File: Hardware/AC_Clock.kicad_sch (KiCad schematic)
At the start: 49 parts, among them J1 L, J2 N, J5 Conn_01x10, J6 Conn_01x10, SW1 Min_PB, SW2 Hr_PB, T1 10:1, U1 AZ1117-5.0, U2 LTV-817S, U3 4040, U4 74LS393, U5 74LS393

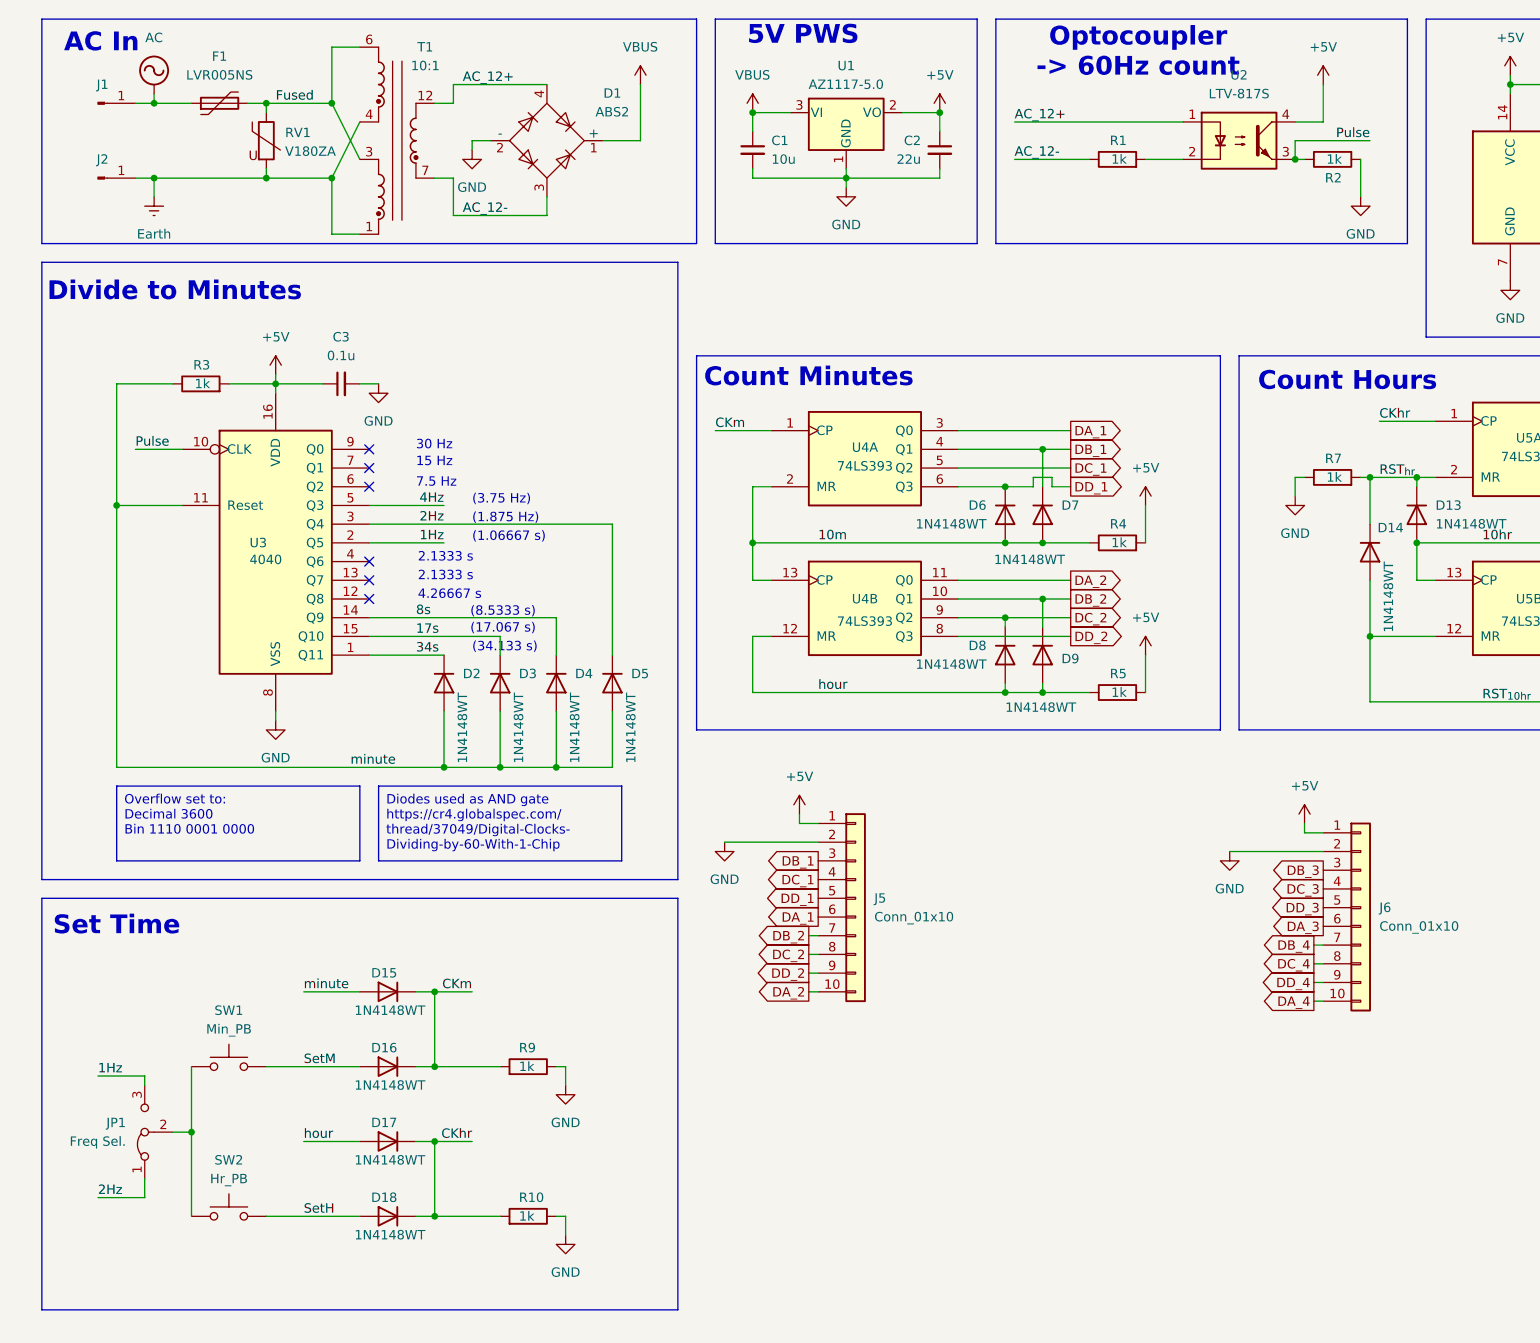
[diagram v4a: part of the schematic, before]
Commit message: Add Class Y Safety capacitor
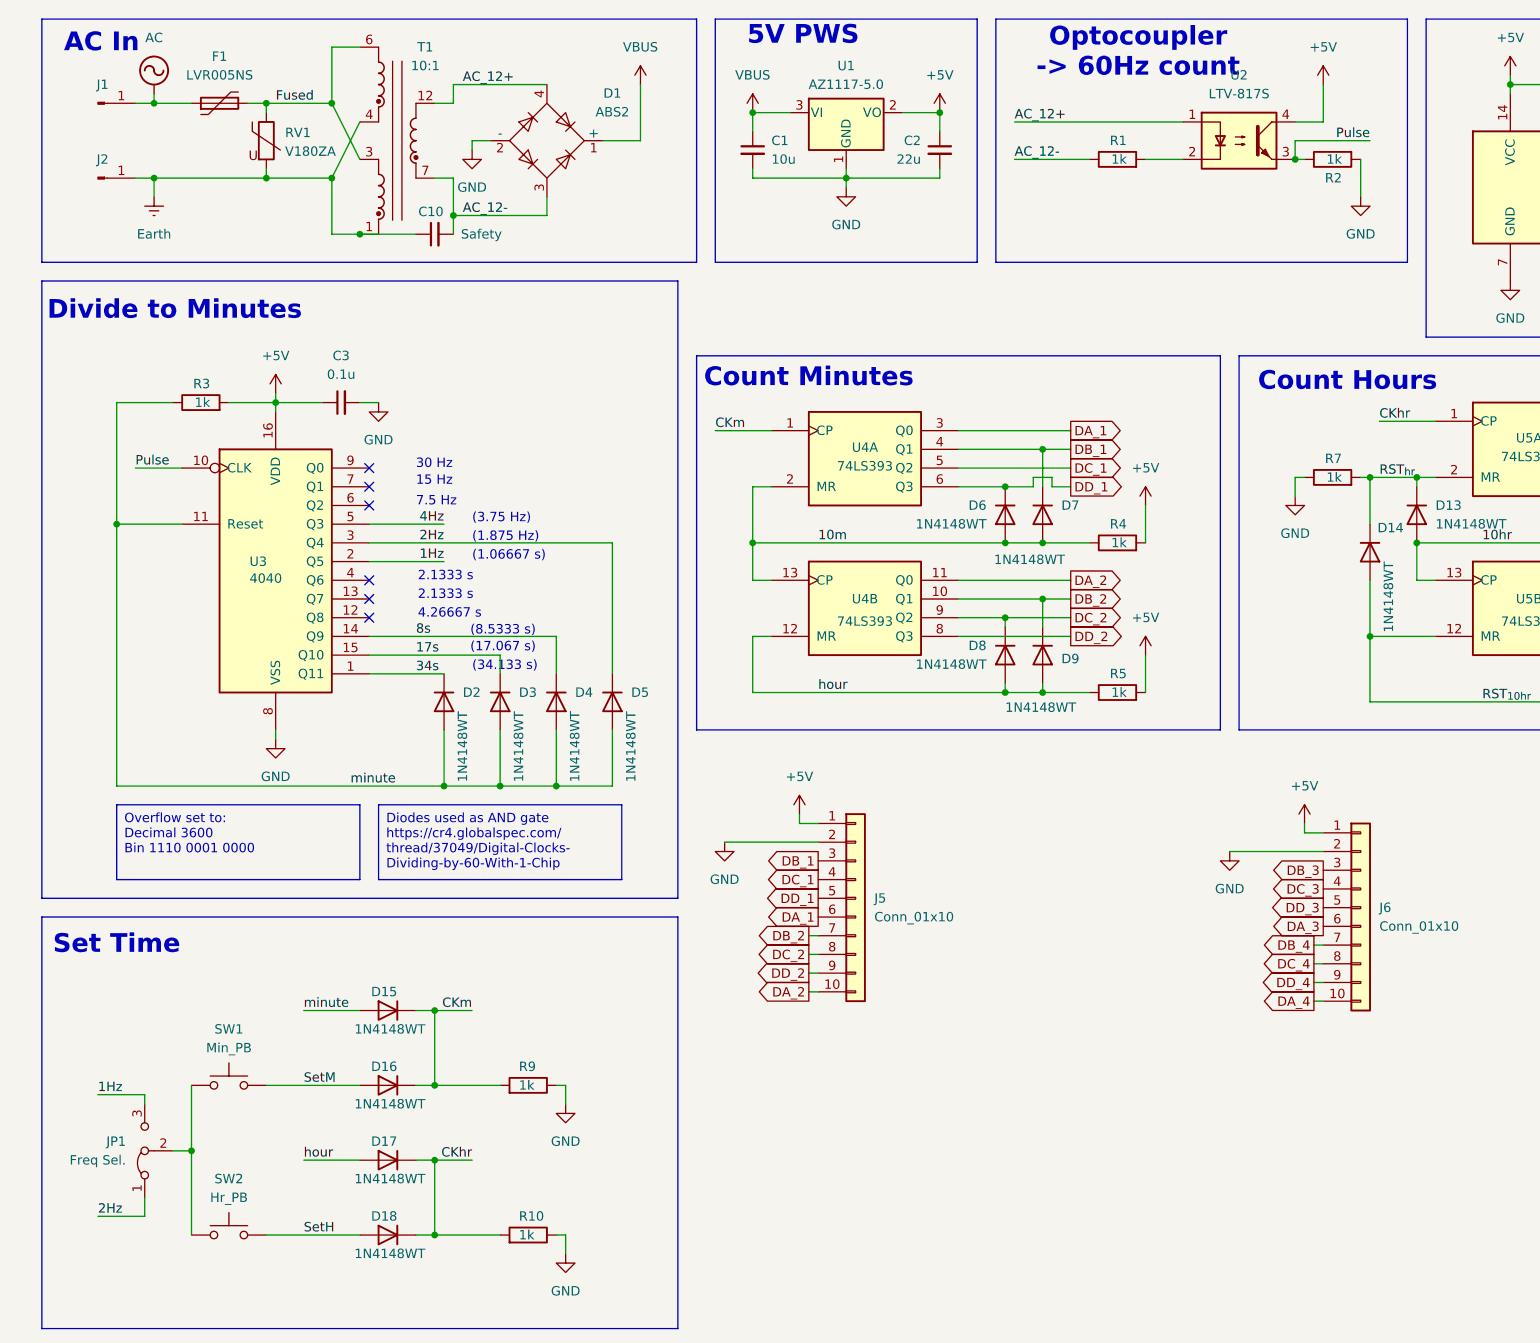
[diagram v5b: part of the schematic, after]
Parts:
- added C10: Safety, Capacitor_THT:C_Disc_D7.5mm_W5.0mm_P7.50mm, symbol Device:C_Small
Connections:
- net AC_12-: now also C10.2
- net Earth: now also C10.1
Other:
- moved on the sheet: C3, D15, D16, D17, D18, D2, D3, D4, D5, JP1, R10, R3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

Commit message: Fix U2 footprint; change to DIP-4
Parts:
- U2: footprint Package_DIP:SMDIP-6_W9.53mm_Clearance8mm -> Package_DIP:SMDIP-4_W9.53mm
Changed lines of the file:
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@@
 			)
 		)
-		(property "Footprint" "Package_DIP:SMDIP-6_W9.53mm_Clearance8mm"
+		(property "Footprint" "Package_DIP:SMDIP-4_W9.53mm"
 			(at 177.8 39.37 0)
 			(effects

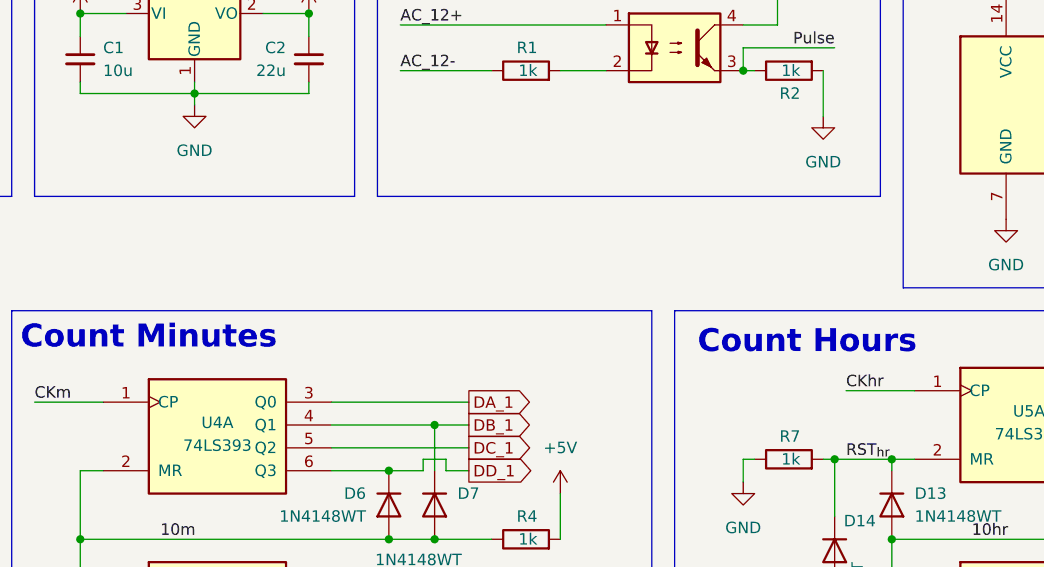
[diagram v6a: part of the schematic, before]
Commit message: Add some notes on what ICs to change and switch Safety Capacitor to Y1 type
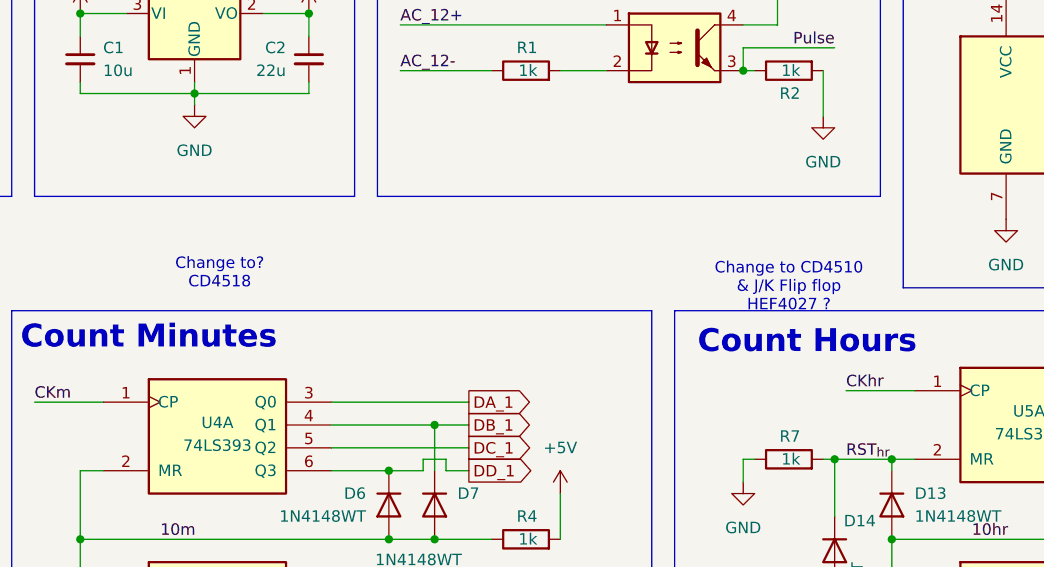
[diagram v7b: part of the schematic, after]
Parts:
- C10: footprint Capacitor_THT:C_Disc_D7.5mm_W5.0mm_P7.50mm -> (none); MPN DE2B3SA221KA3BX02F -> DE1E3RA102MJ4BN01F
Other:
- note added: "Change to CD4510 & J/K Flip flop HEF4027 ?"
- note added: "Change to? CD4518"
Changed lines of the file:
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@@
 		)
 	)
+	(text "Change to?\nCD4518"
+		(exclude_from_sim no)
+		(at 127.254 56.896 0)
+		(effects
+			(font
+				(size 1.27 1.27)
+			)
+		)
+	)
 	(text "(3.75 Hz)"
 		(exclude_from_sim no)
@@
 		)
 	)
+	(text "Change to CD4510\n& J/K Flip flop\nHEF4027 ?"
+		(exclude_from_sim no)
+		(at 190.5 58.42 0)
+		(effects
+			(font
+				(size 1.27 1.27)
+			)
+		)
+	)
 	(text "(1.06667 s)"
 		(exclude_from_sim no)
@@
 			)
 		)
-		(property "Footprint" "Capacitor_THT:C_Disc_D7.5mm_W5.0mm_P7.50mm"
+		(property "Footprint" ""
 			(at 68.58 44.45 0)
 			(effects
@@
 			)
 		)
-		(property "MPN" "DE2B3SA221KA3BX02F"
+		(property "MPN" "DE1E3RA102MJ4BN01F"
 			(at 68.58 44.45 90)
 			(effects

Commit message: Make the IC changes for minute and hour counters
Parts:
- added SW3: Hour Set, symbol Switch:SW_SPDT
- added SW4: Min Set, symbol Switch:SW_SPDT
- added U14: 4518, symbol 4xxx:4518
- added U15: 4510, symbol 4xxx:4510
- added U16: 4027, symbol 4xxx:4027
- added U17: 4081, symbol 4xxx:4081
- J5: value Conn_01x10 -> Minutes
- J6: value Conn_01x10 -> Hours
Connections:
- net +5V: now also U14.16 (VDD), U15.10 (U/D), U15.16 (VDD), U15.4 (A1), U16.10 (J), U16.11 (K), U16.16 (VDD), U16.5 (K), U16.6 (J), U17.14 (VDD)
- net 2Hz: now also SW3.3 (C), SW4.3 (C)
- net DA_1: now also U14.11 (Q1)
- net DA_2: now also U14.3 (Q1)
- net DA_3: now also U15.6 (Q1), U17.9
- net DA_4: no longer J6.10 (Pin_10)
- net DB_1: now also U14.12 (Q2)
- net DB_2: now also U14.4 (Q2), U17.13
- net DB_3: now also U15.11 (Q2), U17.6
- net DB_4: no longer J6.7 (Pin_7)
- net DC_1: now also U14.13 (Q3)
- net DC_2: now also U14.5 (Q3), U17.12
- net DC_3: now also U15.14 (Q3)
- net DC_4: no longer J6.8 (Pin_8)
- net DD_1: now also U14.14 (Q4), U14.2 (Enable)
- net DD_2: now also U14.6 (Q4)
- net DD_3: now also U15.2 (Q4)
- net DD_4: no longer J6.9 (Pin_9)
- net GND: now also U14.1 (CK), U14.15 (Reset), U14.8 (VSS), U14.9 (CK), U15.12 (A2), U15.13 (A3), U15.3 (A4), U15.5 (CI), U15.8 (VSS), U15.9 (RST), U16.12 (R), U16.7 (S), U16.8 (VSS), U16.9 (S), U17.7 (VSS)
- net minute: now also SW4.1 (A)
- new net: SW3.1 (A), U14.7 (Reset), U17.11
- new net: U15.1 (PE), U16.4 (R), U17.10
- new net: SW3.2 (B), U15.15 (CLK)
- new net: U15.7 (CO), U16.3 (C)
- new net: U16.13 (C), U17.4, U17.8
- new net: SW4.2 (B), U14.10 (Enable)
- new net 10Hr: J6.8 (Pin_8), U16.1 (Q), U17.5
- new net PM: J6.9 (Pin_9), U16.14 (~{Q})
- no-connect marks 6 -> 13
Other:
- moved on the sheet: C4, C5, D10, D11, D12, D13, D14, D15, D16, D17, D18, D19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
